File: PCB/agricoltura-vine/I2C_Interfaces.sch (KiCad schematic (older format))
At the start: 10 parts

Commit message: Schematic process
scheamtics laid out for all board subsyhstems, connecting MCU to subsystems still in progress, power yet to be designed.
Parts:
- removed T? (x8): 0705430003, AVR-KiCAD-Lib-Connectors:Shrouded_Pin_Header_Straight_1x04_Pitch2.54mm, symbol AVR-KiCAD-Lib-Connectors:0705430003
- added C? (x2): GRM188R61A106KE69J, AVR-KiCAD-Lib-Capacitors:C0603, symbol AVR-KiCAD-Lib-Capacitors:GRM188R61A106KE69J
- added C? (x2): C0402C104K9PACTU, AVR-KiCAD-Lib-Resistors:R0402, symbol AVR-KiCAD-Lib-Capacitors:C0402C104K9PACTU
- added T? (x8): 0705430003, AVR-KiCAD-Lib-Connectors:Shrouded_Pin_Header_Straight_1x04_Pitch2.54mm, symbol AVR-KiCAD-Lib-Connectors:0705430003
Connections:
- net labels added: +3V3, GND, I2C_MUX1_RESET, I2C_MUX2_RESET, I2C_SENSE1_SCL, I2C_SENSE1_SDA, I2C_SENSE2_SCL, I2C_SENSE2_SDA
- wire segments 0 -> 64

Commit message: 5V Logic, Connector swap, and I2C refactor
Added 5V IO logic, changed connectors over to grove style SMT, I2C refactored to use 8x mux instead fo two 4x mux.
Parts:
- removed C?: C0402C104K9PACTU, AVR-KiCAD-Lib-Resistors:R0402, symbol AVR-KiCAD-Lib-Capacitors:C0402C104K9PACTU
- removed C?: GRM188R61A106KE69J, AVR-KiCAD-Lib-Capacitors:C0603, symbol AVR-KiCAD-Lib-Capacitors:GRM188R61A106KE69J
- removed T? (x8): 0705430003, AVR-KiCAD-Lib-Connectors:Shrouded_Pin_Header_Straight_1x04_Pitch2.54mm, symbol AVR-KiCAD-Lib-Connectors:0705430003
- removed U? (x2): TCA9546APWR, growbox-KiCAD-ICs:PW0016A, symbol AVR-KiCAD-Lib-ICs:TCA9546APWR
- added T? (x8): BM04B-SRSS-TB(LF)(SN), AVR-KiCAD-Lib-Connectors:CONN_BM04B-SRSS-TB(LF)(SN), symbol AVR-KiCAD-Lib-Connectors:BM04B-SRSS-TB(LF)(SN)
- added U?: TCA9548APWR, AVR-KiCAD-Lib-ICs:TCA9548APWR, symbol AVR-KiCAD-Lib-ICs:TCA9548APWR
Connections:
- net labels removed: I2C_MUX2_RESET, I2C_SENSE2_SCL, I2C_SENSE2_SDA
- wire segments 64 -> 96
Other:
- moved on the sheet: C?

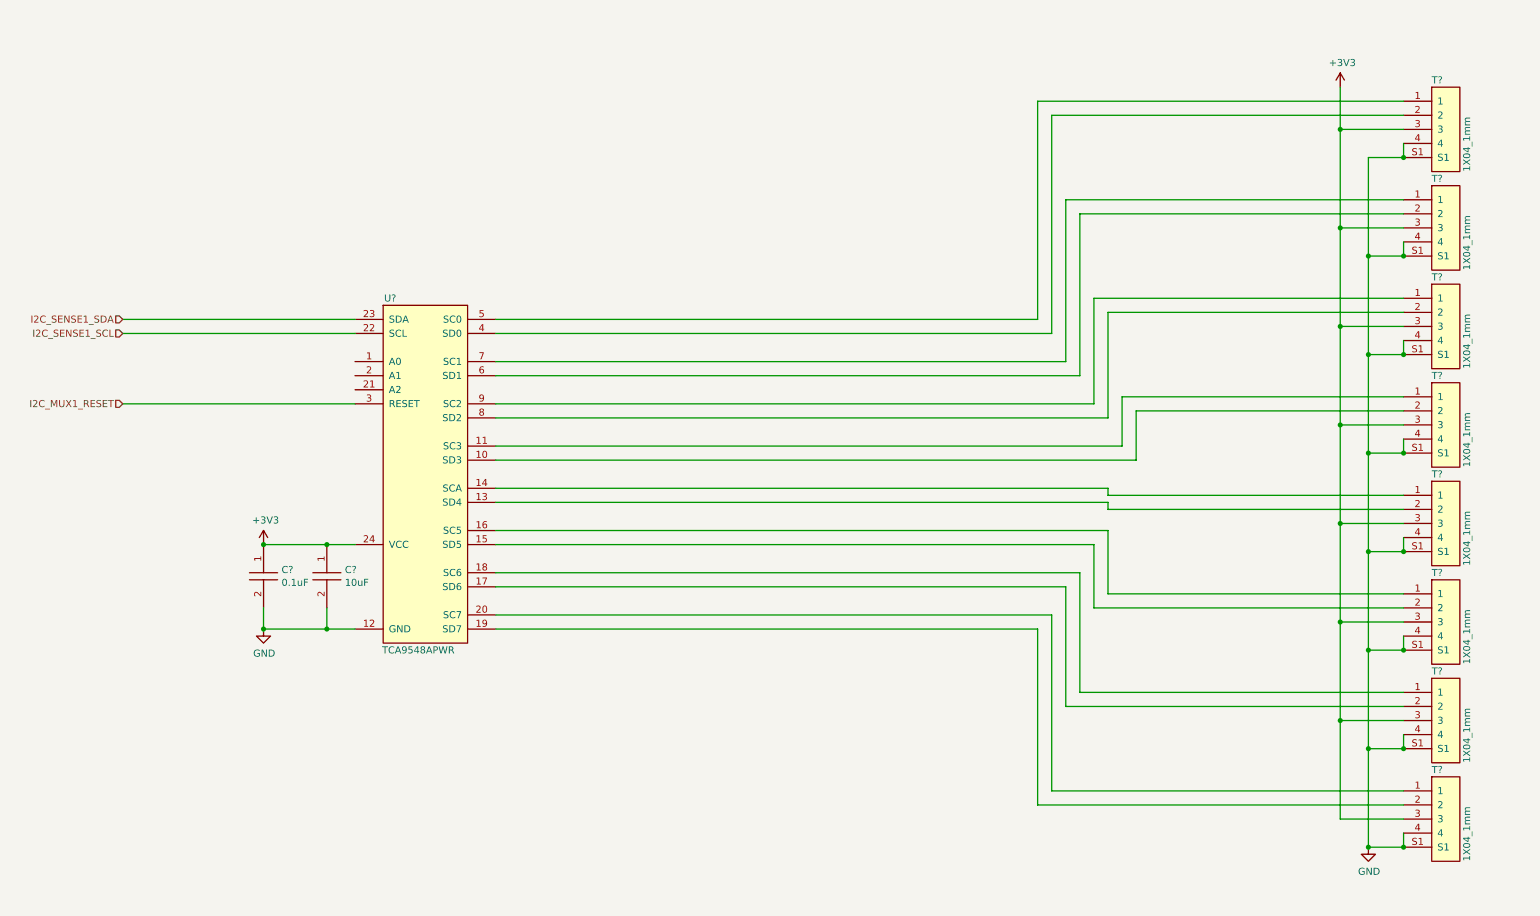
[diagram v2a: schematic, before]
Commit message: Board
Board shape defined, though subject to change. Schematic anotated and parts exported to board.
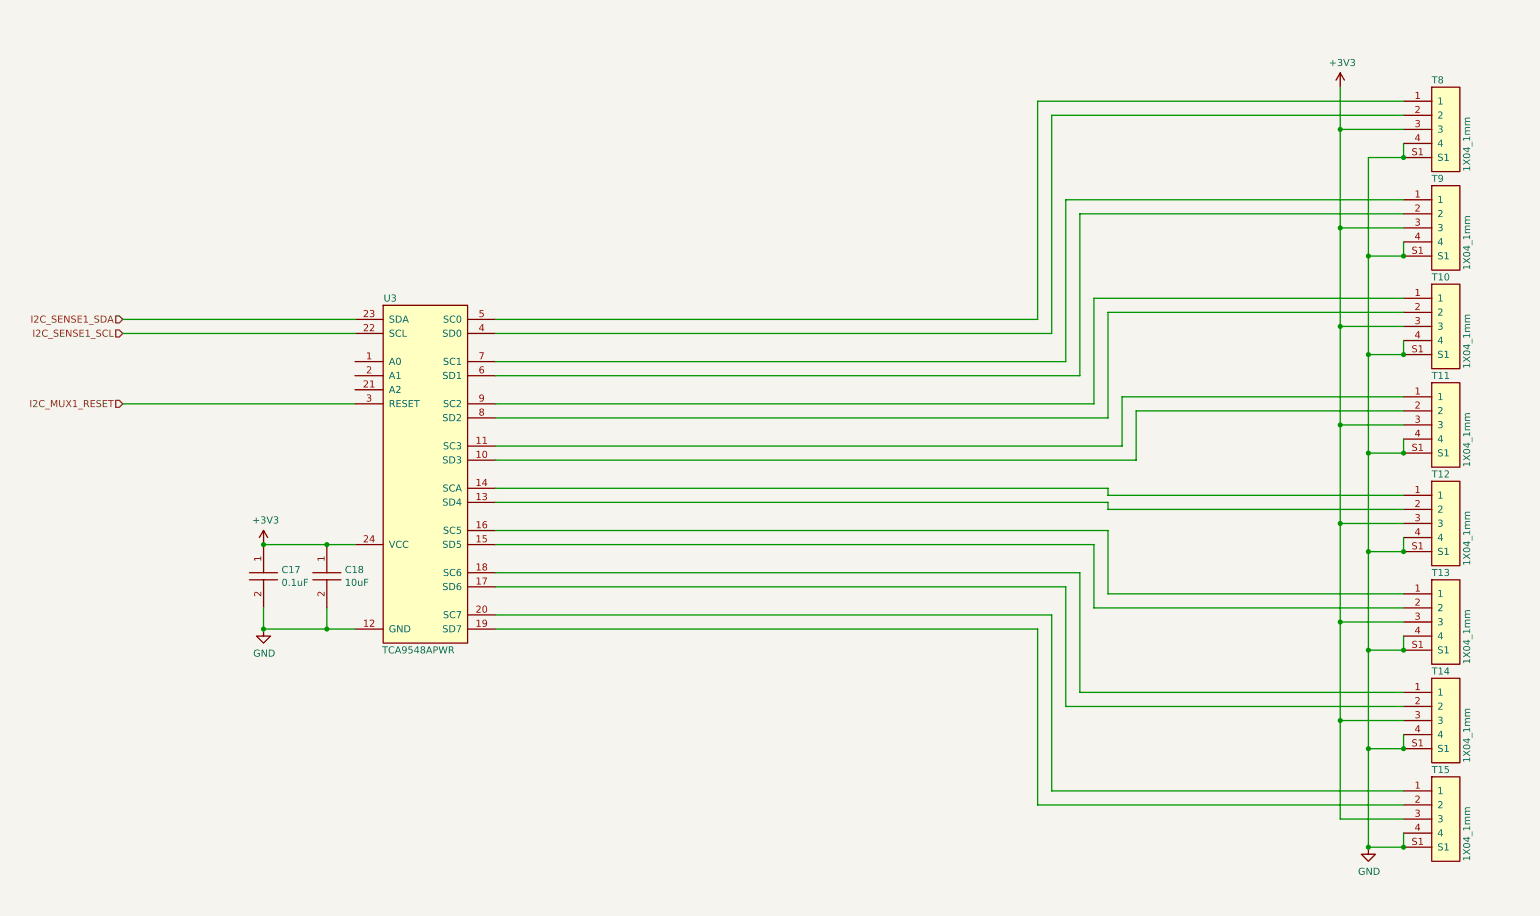
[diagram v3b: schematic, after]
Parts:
- gave numbers to parts that had none: 11
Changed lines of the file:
@@
 P 2900 4250
 AR Path="/5EE82896/5F11563E" Ref="C?"  Part="1"
-AR Path="/5EE827B2/5F11563E" Ref="C?"  Part="1"
-F 0 "C?" V 2879 4378 50  0000 L CNN
+AR Path="/5EE827B2/5F11563E" Ref="C18"  Part="1"
+F 0 "C18" V 2879 4378 50  0000 L CNN
 F 1 "GRM188R61A106KE69J" H 2950 4450 50  0001 C CNN
 F 2 "AVR-KiCAD-Lib-Capacitors:C0603" H 2700 4250 50  0001 C CNN
@@
 P 2450 4050
 AR Path="/5EE82896/5F11561C" Ref="#PWR?"  Part="1"
-AR Path="/5EE827B2/5F11561C" Ref="#PWR?"  Part="1"
-F 0 "#PWR?" H 2450 3900 50  0001 C CNN
+AR Path="/5EE827B2/5F11561C" Ref="#PWR024"  Part="1"
+F 0 "#PWR024" H 2450 3900 50  0001 C CNN
 F 1 "+3V3" H 2465 4223 50  0000 C CNN
 F 2 "" H 2450 4050 50  0001 C CNN
@@
 P 2450 4650
 AR Path="/5EE82896/5F189177" Ref="#PWR?"  Part="1"
-AR Path="/5EE827B2/5F189177" Ref="#PWR?"  Part="1"
-F 0 "#PWR?" H 2450 4400 50  0001 C CNN
+AR Path="/5EE827B2/5F189177" Ref="#PWR025"  Part="1"
+F 0 "#PWR025" H 2450 4400 50  0001 C CNN
 F 1 "GND" H 2455 4477 50  0000 C CNN
 F 2 "" H 2450 4650 50  0001 C CNN
@@
 $EndComp
 $Comp
-L AVR-KiCAD-Lib-ICs:TCA9548APWR U?
+L AVR-KiCAD-Lib-ICs:TCA9548APWR U3
 U 1 1 5EF912D4
 P 3300 2350
-F 0 "U?" H 3350 2400 50  0000 C CNN
+F 0 "U3" H 3350 2400 50  0000 C CNN
 F 1 "TCA9548APWR" H 3350 2550 50  0001 C CNN
 F 2 "AVR-KiCAD-Lib-ICs:TCA9548APWR" H 5650 5050 50  0001 C CNN
@@
 P 10300 6200
 AR Path="/5EE82702/5F0119BE" Ref="#PWR?"  Part="1"
-AR Path="/5EE827B2/5F0119BE" Ref="#PWR?"  Part="1"
-F 0 "#PWR?" H 10300 5950 50  0001 C CNN
+AR Path="/5EE827B2/5F0119BE" Ref="#PWR027"  Part="1"
+F 0 "#PWR027" H 10300 5950 50  0001 C CNN
 F 1 "GND" H 10305 6027 50  0000 C CNN
 F 2 "" H 10300 6200 50  0001 C CNN
@@
 P 10750 800
 AR Path="/5EE82702/5F0119DD" Ref="T?"  Part="1"
-AR Path="/5EE827B2/5F0119DD" Ref="T?"  Part="1"
-F 0 "T?" H 10750 850 50  0000 L CNN
+AR Path="/5EE827B2/5F0119DD" Ref="T8"  Part="1"
+F 0 "T8" H 10750 850 50  0000 L CNN
 F 1 "BM04B-SRSS-TB(LF)(SN)" H 10800 1000 50  0001 C CNN
 F 2 "AVR-KiCAD-Lib-Connectors:CONN_BM04B-SRSS-TB(LF)(SN)" H 9850 1400 50  0001 C CNN
@@
 P 10750 1500
 AR Path="/5EE82702/5F0119FC" Ref="T?"  Part="1"
-AR Path="/5EE827B2/5F0119FC" Ref="T?"  Part="1"
-F 0 "T?" H 10750 1550 50  0000 L CNN
+AR Path="/5EE827B2/5F0119FC" Ref="T9"  Part="1"
+F 0 "T9" H 10750 1550 50  0000 L CNN
 F 1 "BM04B-SRSS-TB(LF)(SN)" H 10800 1700 50  0001 C CNN
 F 2 "AVR-KiCAD-Lib-Connectors:CONN_BM04B-SRSS-TB(LF)(SN)" H 9850 2100 50  0001 C CNN
@@
 P 10750 2200
 AR Path="/5EE82702/5F011A1B" Ref="T?"  Part="1"
-AR Path="/5EE827B2/5F011A1B" Ref="T?"  Part="1"
-F 0 "T?" H 10750 2250 50  0000 L CNN
+AR Path="/5EE827B2/5F011A1B" Ref="T10"  Part="1"
+F 0 "T10" H 10750 2250 50  0000 L CNN
 F 1 "BM04B-SRSS-TB(LF)(SN)" H 10800 2400 50  0001 C CNN
 F 2 "AVR-KiCAD-Lib-Connectors:CONN_BM04B-SRSS-TB(LF)(SN)" H 9850 2800 50  0001 C CNN
@@
 P 10750 2900
 AR Path="/5EE82702/5F011A3A" Ref="T?"  Part="1"
-AR Path="/5EE827B2/5F011A3A" Ref="T?"  Part="1"
-F 0 "T?" H 10750 2950 50  0000 L CNN
+AR Path="/5EE827B2/5F011A3A" Ref="T11"  Part="1"
+F 0 "T11" H 10750 2950 50  0000 L CNN
 F 1 "BM04B-SRSS-TB(LF)(SN)" H 10800 3100 50  0001 C CNN
 F 2 "AVR-KiCAD-Lib-Connectors:CONN_BM04B-SRSS-TB(LF)(SN)" H 9850 3500 50  0001 C CNN
@@
 P 10750 3600
 AR Path="/5EE82702/5F011A59" Ref="T?"  Part="1"
-AR Path="/5EE827B2/5F011A59" Ref="T?"  Part="1"
-F 0 "T?" H 10750 3650 50  0000 L CNN
+AR Path="/5EE827B2/5F011A59" Ref="T12"  Part="1"
+F 0 "T12" H 10750 3650 50  0000 L CNN
 F 1 "BM04B-SRSS-TB(LF)(SN)" H 10800 3800 50  0001 C CNN
 F 2 "AVR-KiCAD-Lib-Connectors:CONN_BM04B-SRSS-TB(LF)(SN)" H 9850 4200 50  0001 C CNN
@@
 P 10750 4300
 AR Path="/5EE82702/5F011A78" Ref="T?"  Part="1"
-AR Path="/5EE827B2/5F011A78" Ref="T?"  Part="1"
-F 0 "T?" H 10750 4350 50  0000 L CNN
+AR Path="/5EE827B2/5F011A78" Ref="T13"  Part="1"
+F 0 "T13" H 10750 4350 50  0000 L CNN
 F 1 "BM04B-SRSS-TB(LF)(SN)" H 10800 4500 50  0001 C CNN
 F 2 "AVR-KiCAD-Lib-Connectors:CONN_BM04B-SRSS-TB(LF)(SN)" H 9850 4900 50  0001 C CNN
@@
 P 10750 5000
 AR Path="/5EE82702/5F011A97" Ref="T?"  Part="1"
-AR Path="/5EE827B2/5F011A97" Ref="T?"  Part="1"
-F 0 "T?" H 10750 5050 50  0000 L CNN
+AR Path="/5EE827B2/5F011A97" Ref="T14"  Part="1"
+F 0 "T14" H 10750 5050 50  0000 L CNN
 F 1 "BM04B-SRSS-TB(LF)(SN)" H 10800 5200 50  0001 C CNN
 F 2 "AVR-KiCAD-Lib-Connectors:CONN_BM04B-SRSS-TB(LF)(SN)" H 9850 5600 50  0001 C CNN
@@
 P 10750 5700
 AR Path="/5EE82702/5F011AB6" Ref="T?"  Part="1"
-AR Path="/5EE827B2/5F011AB6" Ref="T?"  Part="1"
-F 0 "T?" H 10750 5750 50  0000 L CNN
+AR Path="/5EE827B2/5F011AB6" Ref="T15"  Part="1"
+F 0 "T15" H 10750 5750 50  0000 L CNN
 F 1 "BM04B-SRSS-TB(LF)(SN)" H 10800 5900 50  0001 C CNN
 F 2 "AVR-KiCAD-Lib-Connectors:CONN_BM04B-SRSS-TB(LF)(SN)" H 9850 6300 50  0001 C CNN
@@
 P 2450 4250
 AR Path="/5EE82896/5F11565D" Ref="C?"  Part="1"
-AR Path="/5EE827B2/5F11565D" Ref="C?"  Part="1"
-F 0 "C?" V 2429 4378 50  0000 L CNN
+AR Path="/5EE827B2/5F11565D" Ref="C17"  Part="1"
+F 0 "C17" V 2429 4378 50  0000 L CNN
 F 1 "C0402C104K9PACTU" H 2500 4450 50  0001 C CNN
 F 2 "AVR-KiCAD-Lib-Resistors:R0402" H 2250 4250 50  0001 C CNN
@@
 P 10100 800
 AR Path="/5EE82896/5F11A0D2" Ref="#PWR?"  Part="1"
-AR Path="/5EE827B2/5F11A0D2" Ref="#PWR?"  Part="1"
-F 0 "#PWR?" H 10100 650 50  0001 C CNN
+AR Path="/5EE827B2/5F11A0D2" Ref="#PWR026"  Part="1"
+F 0 "#PWR026" H 10100 650 50  0001 C CNN
 F 1 "+3V3" H 10115 973 50  0000 C CNN
 F 2 "" H 10100 800 50  0001 C CNN

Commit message: Board Size , Connectors and Layout
Changed board size and shape, started layout, swapped connectors over.
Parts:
- removed T10, T11, T12, T13, T14, T15, T8, T9: BM04B-SRSS-TB(LF)(SN), AVR-KiCAD-Lib-Connectors:CONN_BM04B-SRSS-TB(LF)(SN), symbol AVR-KiCAD-Lib-Connectors:BM04B-SRSS-TB(LF)(SN)
- added T10, T11, T12, T13, T14, T15, T8, T9: B4B-PH-K-S(LF)(SN), AVR-KiCAD-Lib-Connectors:B4B-PH-K-S(LF)(SN), symbol AVR-KiCAD-Lib-Connectors:B4B-PH-K-S(LF)(SN)

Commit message: Route Started Connectors Changed
Changed to QWIIC style connectors and adjusted pinning of RJ45s, but switching to screw terminal header in next commit. THis is a backup
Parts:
- removed T10, T11, T12, T13, T14, T15, T8, T9: B4B-PH-K-S(LF)(SN), AVR-KiCAD-Lib-Connectors:B4B-PH-K-S(LF)(SN), symbol AVR-KiCAD-Lib-Connectors:B4B-PH-K-S(LF)(SN)
- added T10, T11, T12, T13, T14, T15, T8, T9: BM04B-SRSS-TB(LF)(SN), AVR-KiCAD-Lib-Connectors:CONN_BM04B-SRSS-TB(LF)(SN), symbol AVR-KiCAD-Lib-Connectors:BM04B-SRSS-TB(LF)(SN)

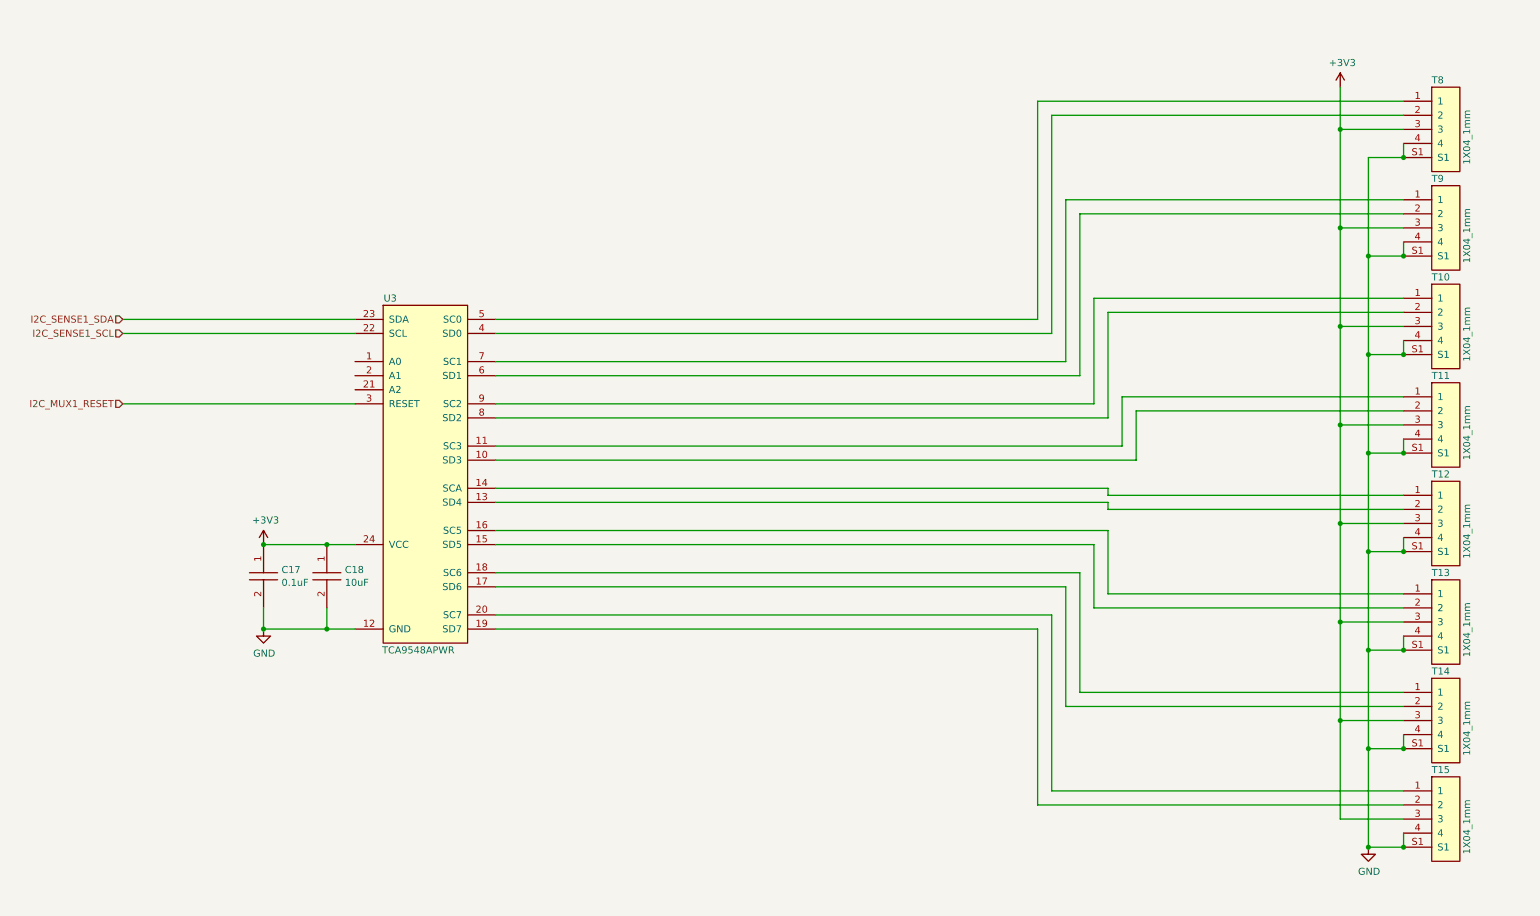
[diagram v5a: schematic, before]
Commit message: Majopr Progress
Board shape enlarged to simplify layout and accomodate larger size parts for sisterboard like Ivy. QWIIC connectors flipped to be correct, signals were oriented incorrectly in past revisions.
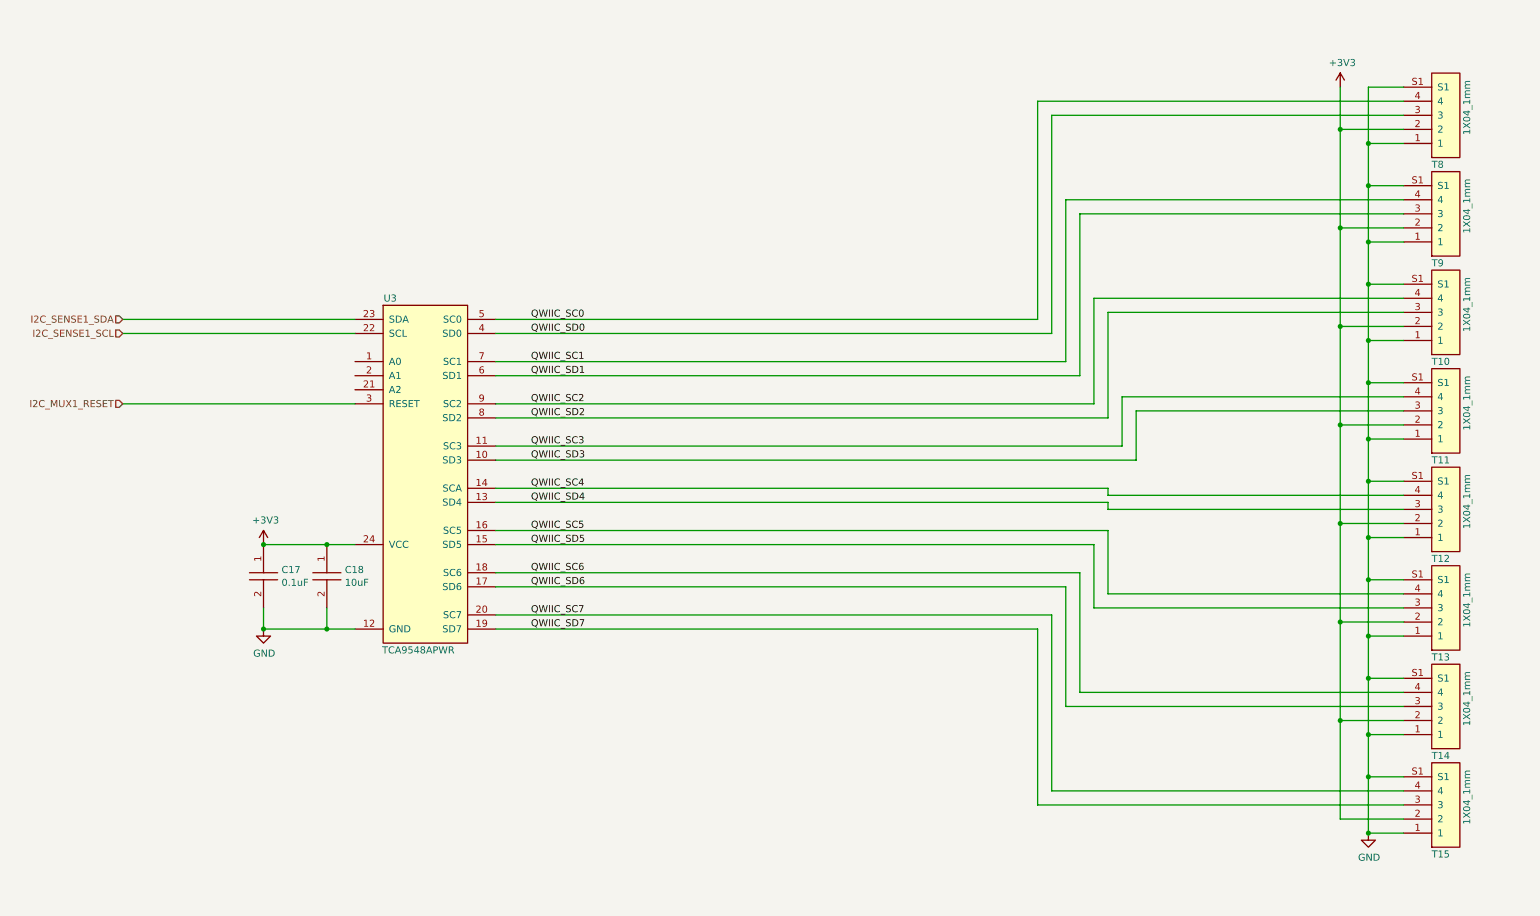
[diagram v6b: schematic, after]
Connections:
- net +3V3: now also T10.2, T11.2, T12.2, T13.2, T14.2, T15.2, T8.2, T9.2; no longer T10.3, T11.3, T12.3, T13.3, T14.3, T15.3, T8.3, T9.3
- net GND: now also T10.1, T11.1, T12.1, T13.1, T14.1, T15.1, T8.1, T9.1; no longer T10.4, T11.4, T12.4, T13.4, T14.4, T15.4, T8.4, T9.4
- net QWIIC_SC0: now reaches U3.5 (SC0)
- net QWIIC_SC0: now also T8.4; no longer T8.1
- net QWIIC_SD0: now reaches U3.4 (SD0)
- net QWIIC_SD0: now also T8.3; no longer T8.2
- net QWIIC_SC1: now reaches U3.7 (SC1)
- net QWIIC_SC1: now also T9.4; no longer T9.1
- net QWIIC_SD1: now reaches U3.6 (SD1)
- net QWIIC_SD1: now also T9.3; no longer T9.2
- net QWIIC_SC2: now reaches U3.9 (SC2)
- net QWIIC_SC2: now also T10.4; no longer T10.1
- net QWIIC_SD2: now reaches U3.8 (SD2)
- net QWIIC_SD2: now also T10.3; no longer T10.2
- net QWIIC_SC3: now reaches U3.11 (SC3)
- net QWIIC_SC3: now also T11.4; no longer T11.1
- net QWIIC_SD3: now reaches U3.10 (SD3)
- net QWIIC_SD3: now also T11.3; no longer T11.2
- net QWIIC_SC4: now reaches U3.14 (SCA)
- net QWIIC_SC4: now also T12.4; no longer T12.1
- net QWIIC_SD4: now reaches U3.13 (SD4)
- net QWIIC_SD4: now also T12.3; no longer T12.2
- net QWIIC_SC5: now reaches U3.16 (SC5)
- net QWIIC_SC5: now also T13.4; no longer T13.1
- net QWIIC_SD5: now reaches U3.15 (SD5)
- net QWIIC_SD5: now also T13.3; no longer T13.2
- net QWIIC_SC6: now reaches U3.18 (SC6)
- net QWIIC_SC6: now also T14.4; no longer T14.1
- net QWIIC_SD6: now reaches U3.17 (SD6)
- net QWIIC_SD6: now also T14.3; no longer T14.2
- net QWIIC_SC7: now reaches U3.20 (SC7)
- net QWIIC_SC7: now also T15.4; no longer T15.1
- net QWIIC_SD7: now reaches U3.19 (SD7)
- net QWIIC_SD7: now also T15.3; no longer T15.2
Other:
- moved on the sheet: T10, T11, T12, T13, T14, T15, T8, T9
